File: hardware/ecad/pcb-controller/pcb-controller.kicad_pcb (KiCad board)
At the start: 2 copper layers, 50 x 40 mm, 27 parts, among them J1 Conn_01x05, J2 Conn_01x05, J3 Conn_02x16_Row_Letter_Last, U1 PCA9685BS

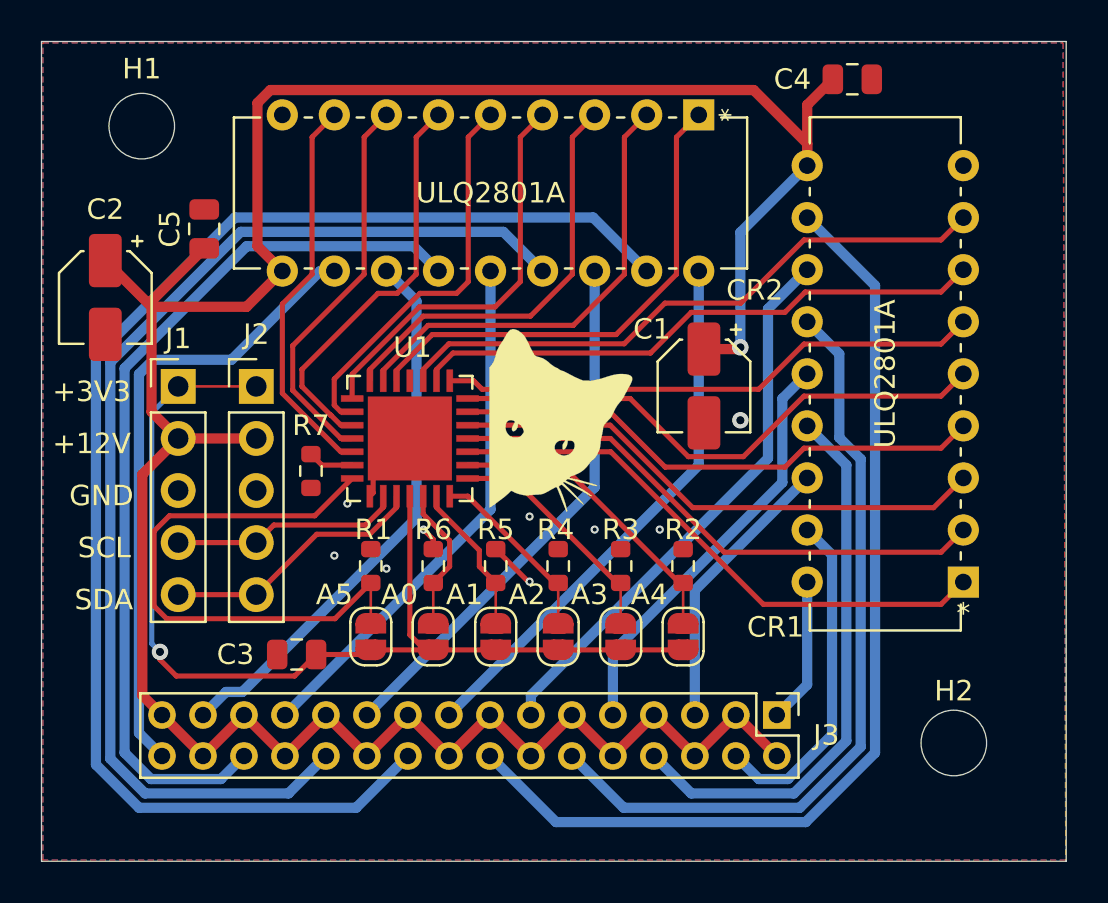
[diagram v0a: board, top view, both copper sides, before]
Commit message: Switched to 16 pin header from 32 pin connector. Updated gerber.
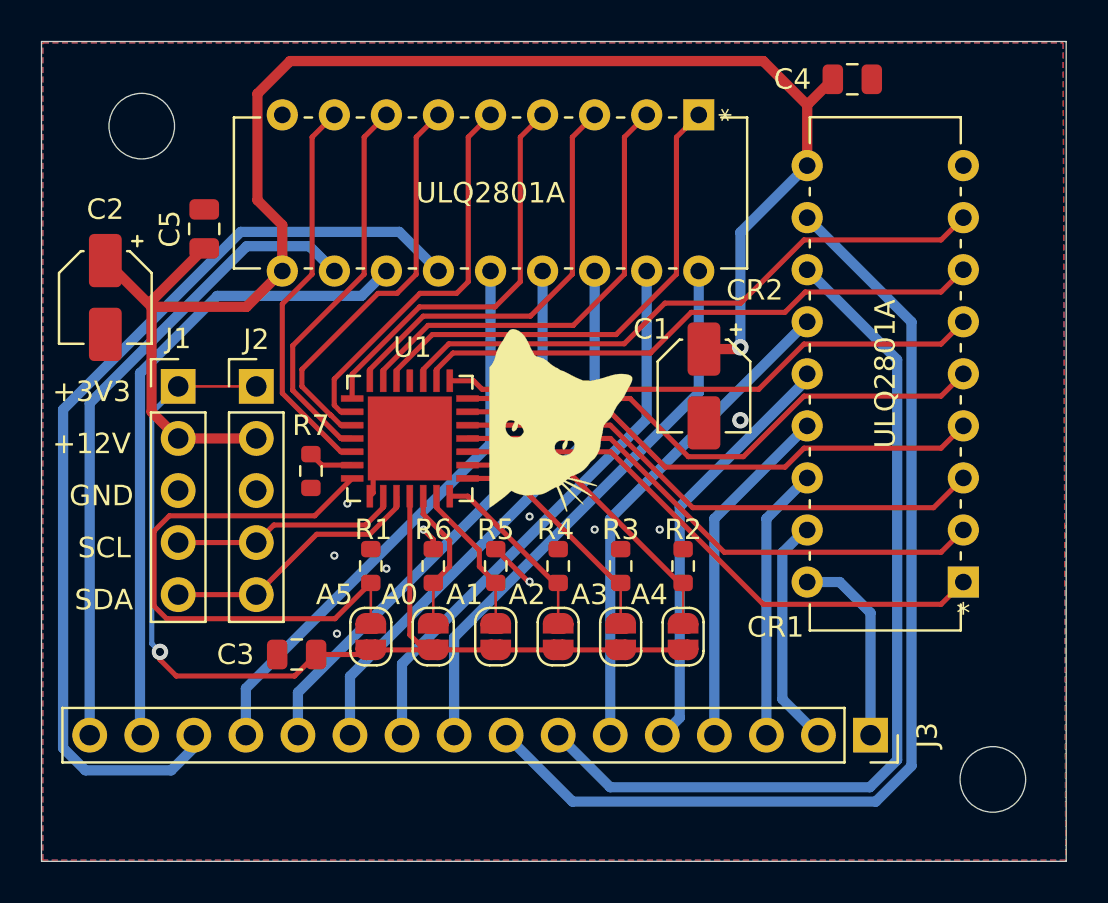
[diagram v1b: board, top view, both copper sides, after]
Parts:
- J3: value Conn_02x16_Row_Letter_Last -> Conn_01x16; footprint Connector_PinHeader_2.00mm:PinHeader_2x16_P2.00mm_Vertical -> Connector_PinSocket_2.54mm:PinSocket_1x16_P2.54mm_Vertical
- moved J3 4.68 mm to (60.5, 53.8)
- moved H2 2.61 mm to (66.4, 56.0)
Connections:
- J3 pad 10: +12V -> Net-(CR2-Pad17)
- J3 pad 11: +12V -> Net-(CR2-Pad16)
- J3 pad 12: Net-(CR1-Pad13) -> Net-(CR2-Pad15)
- J3 pad 13: Net-(CR1-Pad12) -> Net-(CR2-Pad14)
- J3 pad 14: +12V -> Net-(CR2-Pad13)
- J3 pad 15: +12V -> Net-(CR2-Pad12)
- J3 pad 16: Net-(CR1-Pad11) -> Net-(CR2-Pad11)
- J3 pad 2: +12V -> Net-(CR1-Pad17)
- J3 pad 3: +12V -> Net-(CR1-Pad16)
- J3 pad 4: Net-(CR1-Pad17) -> Net-(CR1-Pad15)
- J3 pad 5: Net-(CR1-Pad16) -> Net-(CR1-Pad14)
- J3 pad 6: +12V -> Net-(CR1-Pad13)
- J3 pad 7: +12V -> Net-(CR1-Pad12)
- J3 pad 8: Net-(CR1-Pad15) -> Net-(CR1-Pad11)
- J3 pad 9: Net-(CR1-Pad14) -> Net-(CR2-Pad18)
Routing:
- net +12V: track 136.7 -> 79.3 mm
- net Net-(CR2-Pad17): track 67.8 -> 27.6 mm
- net Net-(CR2-Pad15): track 55.8 -> 27.6 mm
- net Net-(CR1-Pad12): track 27.3 -> 43.9 mm
- net Net-(CR1-Pad13): track 38.2 -> 24.2 mm
- net Net-(CR1-Pad15): track 27.4 -> 17.0 mm
- net Net-(CR1-Pad17): track 16.6 -> 11.3 mm
- net Net-(CR2-Pad12): track 27.1 -> 31.8 mm
- net Net-(CR2-Pad13): track 43.9 -> 47.1 mm
- net Net-(CR1-Pad18): track 7.10 -> 9.68 mm
- net Net-(CR2-Pad14): track 25.8 -> 27.6 mm
- net Net-(CR1-Pad11): track 49.0 -> 50.7 mm
- net Net-(CR2-Pad16): track 26.3 -> 27.9 mm
- net Net-(CR2-Pad11): track 30.7 -> 31.8 mm
- net Net-(CR2-Pad18): track 26.7 -> 27.6 mm
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
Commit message: Fixed symbol libraries.
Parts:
- J3: footprint Connector_PinSocket_2.54mm:PinSocket_1x16_P2.54mm_Vertical -> Connector_PinHeader_2.54mm:PinHeader_1x16_P2.54mm_Vertical
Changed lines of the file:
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@@
   (page A4)
   (layers
-    (0 F.Cu signal hide)
-    (31 B.Cu signal hide)
+    (0 F.Cu signal)
+    (31 B.Cu signal)
     (32 B.Adhes user)
     (33 F.Adhes user)
@@
     (add_net "Net-(R7-Pad1)")
   )
-  (module Connector_PinSocket_2.54mm:PinSocket_1x16_P2.54mm_Vertical (layer F.Cu)
+  (module Connector_PinHeader_2.54mm:PinHeader_1x16_P2.54mm_Vertical (layer F.Cu)
     (at 60.452 53.848 270)
-    (descr "Through hole straight socket strip, 1x16, 2.54mm pitch, single row (from Kicad 4.0.7), script generated")
-    (tags "Through hole socket strip THT 1x16 2.54mm single row")
-    (fp_text reference J3 (at 0 -2.77 90) (layer F.SilkS)
+    (descr "Through hole straight pin header, 1x16, 2.54mm pitch, single row")
+    (tags "Through hole pin header THT 1x16 2.54mm single row")
+    (fp_text reference J3 (at 0 -2.33 90) (layer F.SilkS)
       (effects (font (size 1 1) (thickness 0.15)))
     )
-    (fp_text value Conn_01x16 (at 0 40.87 90) (layer F.Fab)
+    (fp_text value Conn_01x16 (at 0 40.43 90) (layer F.Fab)
       (effects (font (size 1 1) (thickness 0.15)))
     )
@@
       (effects (font (size 1 1) (thickness 0.15)))
     )
-    (fp_line (start -1.27 -1.27) (end 0.635 -1.27) (layer F.Fab) (width 0.1))
-    (fp_line (start 0.635 -1.27) (end 1.27 -0.635) (layer F.Fab) (width 0.1))
-    (fp_line (start 1.27 -0.635) (end 1.27 39.37) (layer F.Fab) (width 0.1))
+    (fp_line (start -0.635 -1.27) (end 1.27 -1.27) (layer F.Fab) (width 0.1))
+    (fp_line (start 1.27 -1.27) (end 1.27 39.37) (layer F.Fab) (width 0.1))
     (fp_line (start 1.27 39.37) (end -1.27 39.37) (layer F.Fab) (width 0.1))
-    (fp_line (start -1.27 39.37) (end -1.27 -1.27) (layer F.Fab) (width 0.1))
+    (fp_line (start -1.27 39.37) (end -1.27 -0.635) (layer F.Fab) (width 0.1))
+    (fp_line (start -1.27 -0.635) (end -0.635 -1.27) (layer F.Fab) (width 0.1))
+    (fp_line (start -1.33 39.43) (end 1.33 39.43) (layer F.SilkS) (width 0.12))
+    (fp_line (start -1.33 1.27) (end -1.33 39.43) (layer F.SilkS) (width 0.12))
+    (fp_line (start 1.33 1.27) (end 1.33 39.43) (layer F.SilkS) (width 0.12))
     (fp_line (start -1.33 1.27) (end 1.33 1.27) (layer F.SilkS) (width 0.12))
-    (fp_line (start -1.33 1.27) (end -1.33 39.43) (layer F.SilkS) (width 0.12))
-    (fp_line (start -1.33 39.43) (end 1.33 39.43) (layer F.SilkS) (width 0.12))
-    (fp_line (start 1.33 1.27) (end 1.33 39.43) (layer F.SilkS) (width 0.12))
-    (fp_line (start 1.33 -1.33) (end 1.33 0) (layer F.SilkS) (width 0.12))
-    (fp_line (start 0 -1.33) (end 1.33 -1.33) (layer F.SilkS) (width 0.12))
-    (fp_line (start -1.8 -1.8) (end 1.75 -1.8) (layer F.CrtYd) (width 0.05))
-    (fp_line (start 1.75 -1.8) (end 1.75 39.9) (layer F.CrtYd) (width 0.05))
-    (fp_line (start 1.75 39.9) (end -1.8 39.9) (layer F.CrtYd) (width 0.05))
-    (fp_line (start -1.8 39.9) (end -1.8 -1.8) (layer F.CrtYd) (width 0.05))
+    (fp_line (start -1.33 0) (end -1.33 -1.33) (layer F.SilkS) (width 0.12))
+    (fp_line (start -1.33 -1.33) (end 0 -1.33) (layer F.SilkS) (width 0.12))
+    (fp_line (start -1.8 -1.8) (end -1.8 39.9) (layer F.CrtYd) (width 0.05))
+    (fp_line (start -1.8 39.9) (end 1.8 39.9) (layer F.CrtYd) (width 0.05))
+    (fp_line (start 1.8 39.9) (end 1.8 -1.8) (layer F.CrtYd) (width 0.05))
+    (fp_line (start 1.8 -1.8) (end -1.8 -1.8) (layer F.CrtYd) (width 0.05))
     (pad 16 thru_hole oval (at 0 38.1 270) (size 1.7 1.7) (drill 1) (layers *.Cu *.Mask)
       (net 38 "Net-(CR2-Pad11)"))
@@
     (pad 1 thru_hole rect (at 0 0 270) (size 1.7 1.7) (drill 1) (layers *.Cu *.Mask)
       (net 23 "Net-(CR1-Pad18)"))
-    (model ${KISYS3DMOD}/Connector_PinSocket_2.54mm.3dshapes/PinSocket_1x16_P2.54mm_Vertical.wrl
+    (model ${KISYS3DMOD}/Connector_PinHeader_2.54mm.3dshapes/PinHeader_1x16_P2.54mm_Vertical.wrl
       (at (xyz 0 0 0))
       (scale (xyz 1 1 1))
